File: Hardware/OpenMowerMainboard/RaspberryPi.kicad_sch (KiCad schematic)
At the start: 8 parts, among them J16 Conn_02x03_Odd_Even, J4 RPi_GPIO, M1 Fan, Q3 BSS138, U3 SIP32509DT

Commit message: added footprints to schematic
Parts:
- removed J16: Conn_02x03_Odd_Even, Connector_PinHeader_2.54mm:PinHeader_2x03_P2.54mm_Vertical, symbol Connector_Generic:Conn_02x03_Odd_Even
- removed J4: RPi_GPIO, Connector_PinSocket_2.54mm:PinSocket_2x20_P2.54mm_Vertical_SMD, symbol OpenMowerMainboard-rescue:RPi_GPIO-RPi_Hat
- added J21: Raspberry_Pi_2_3, Connector_PinSocket_2.54mm:PinSocket_2x20_P2.54mm_Vertical_SMD, symbol Connector:Raspberry_Pi_2_3
- added J22: Conn_02x03_Odd_Even, Connector_PinHeader_2.54mm:PinHeader_2x03_P2.54mm_Vertical, symbol Connector_Generic:Conn_02x03_Odd_Even
- D1: footprint (none) -> Diode_SMD:D_SOD-123F
- M1: footprint (none) -> Connector_JST:JST_XH_B2B-XH-A_1x02_P2.50mm_Vertical
- R4, R5: footprint Resistor_SMD:R_0805_2012Metric -> Resistor_SMD:R_0805_2012Metric_Pad1.20x1.40mm_HandSolder
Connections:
- net GND: now also J21.14 (GND), J21.20 (GND), J21.25 (GND), J21.30 (GND), J21.34 (GND), J21.39 (GND), J21.6 (GND), J21.9 (GND)
- net PICO_RESET: now also J22.6 (Pin_6)
- net PICO_SWCLK: now also J22.2 (Pin_2)
- net PICO_SWDIO: now also J22.4 (Pin_4)
- net RASPI_FAN_ON: now also J21.31 (GCLK2/GPIO6)
- net RASPI_POWER: now also J21.2 (5V), J21.4 (5V)
- net UART0_RXD: now also J21.10 (GPIO15/RXD)
- net UART0_TXD: now also J21.8 (GPIO14/TXD)
- net UART1_RXD: now also J21.28 (ID_SC/GPIO1)
- net UART1_TXD: now also J21.27 (ID_SD/GPIO0)
- net UART2_RXD: now also J21.29 (GCLK1/GPIO5)
- net UART2_TXD: now also J21.7 (GCLK0/GPIO4)
- net UART3_RXD: now also J21.21 (MISO0/GPIO9)
- net UART3_TXD: now also J21.24 (~{CE0}/GPIO8)
- net UART4_RXD: now also J21.33 (PWM1/GPIO13)
- net UART4_TXD: now also J21.32 (PWM0/GPIO12)
- new net: J21.22 (GPIO25), J22.1 (Pin_1)
- new net: J21.18 (GPIO24), J22.3 (Pin_3)
- new net: J21.16 (GPIO23), J22.5 (Pin_5)
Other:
- note removed: "Thru-Hole Connector"

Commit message: wip
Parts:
- M1: footprint Connector_JST:JST_XH_B2B-XH-A_1x02_P2.50mm_Vertical -> Connector_PinHeader_2.54mm:PinHeader_1x02_P2.54mm_Vertical
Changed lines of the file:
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@@
       (effects (font (size 1.27 1.27)) (justify left))
     )
-    (property "Footprint" "Connector_JST:JST_XH_B2B-XH-A_1x02_P2.50mm_Vertical" (id 2) (at 116.84 36.576 0)
+    (property "Footprint" "Connector_PinHeader_2.54mm:PinHeader_1x02_P2.54mm_Vertical" (id 2) (at 116.84 36.576 0)
       (effects (font (size 1.27 1.27)) hide)
     )

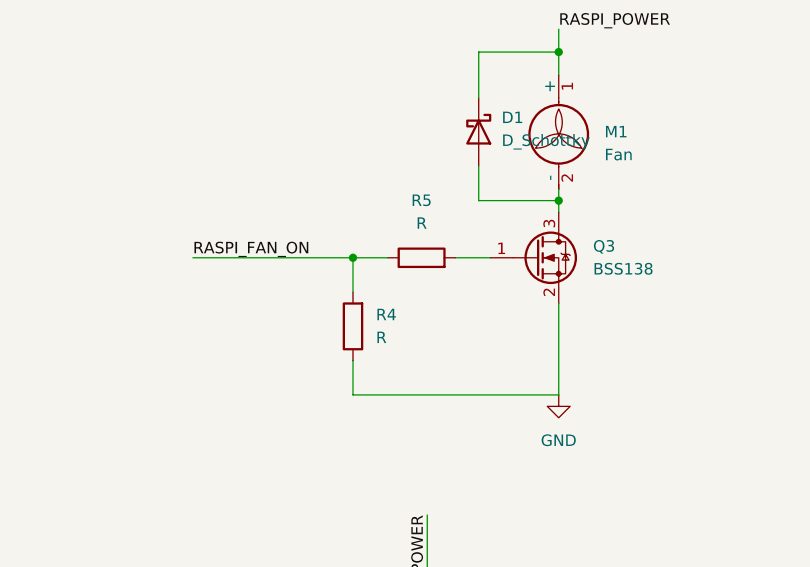
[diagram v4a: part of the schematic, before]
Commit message: update Resistance Values
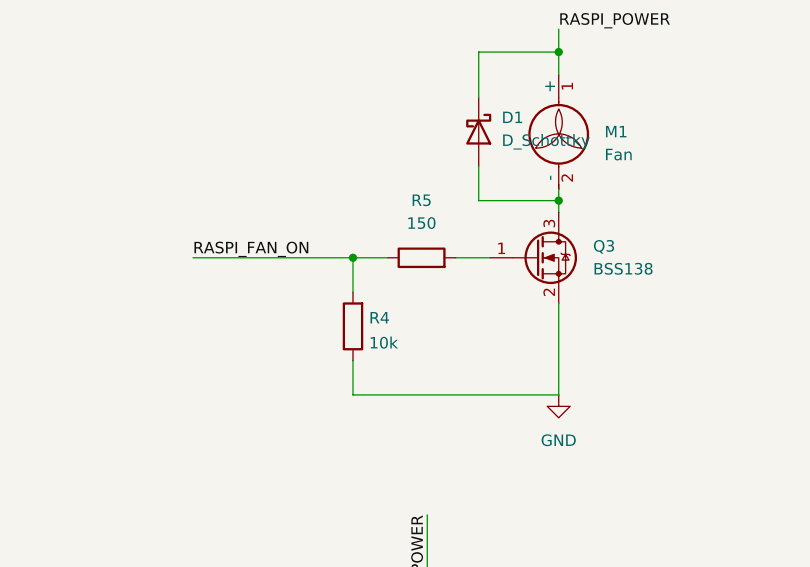
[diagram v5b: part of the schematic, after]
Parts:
- R4: value R -> 10k
- R5: value R -> 150
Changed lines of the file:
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@@
     (in_bom yes) (on_board yes) (fields_autoplaced)
     (property "Reference" "R5" (id 0) (at 101.6 43.18 90))
-    (property "Value" "R" (id 1) (at 101.6 45.72 90))
+    (property "Value" "150" (id 1) (at 101.6 45.72 90))
     (property "Footprint" "Resistor_SMD:R_0805_2012Metric_Pad1.20x1.40mm_HandSolder" (id 2) (at 101.6 51.308 90)
       (effects (font (size 1.27 1.27)) hide)
@@
   (symbol (lib_id "Device:R") (at 93.98 57.15 180) (unit 1)
     (in_bom yes) (on_board yes) (fields_autoplaced)
-    (property "Reference" "R4" (id 0) (at 96.52 55.8799 0)
+    (property "Reference" "R4" (id 0) (at 95.758 56.2415 0)
       (effects (font (size 1.27 1.27)) (justify right))
     )
-    (property "Value" "R" (id 1) (at 96.52 58.4199 0)
+    (property "Value" "10k" (id 1) (at 95.758 59.0166 0)
       (effects (font (size 1.27 1.27)) (justify right))
     )

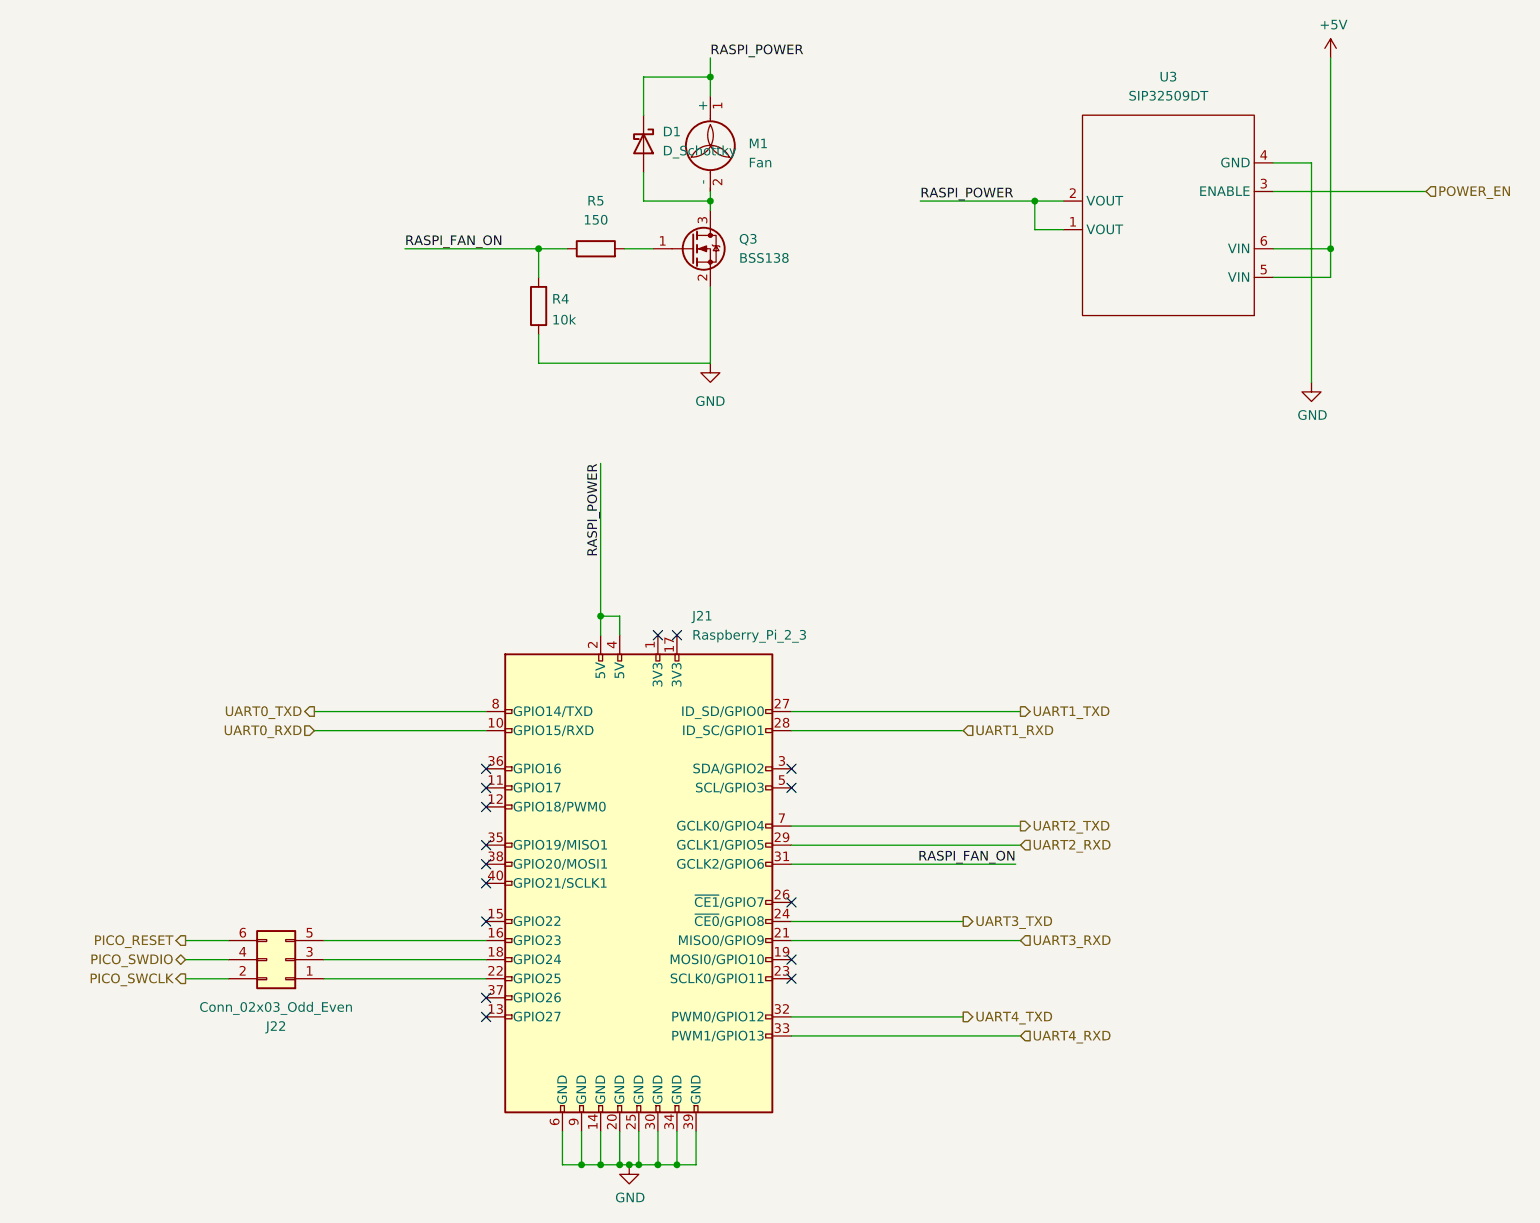
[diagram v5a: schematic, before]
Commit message: Added default pull down, raspberry pi power override and some TODOs
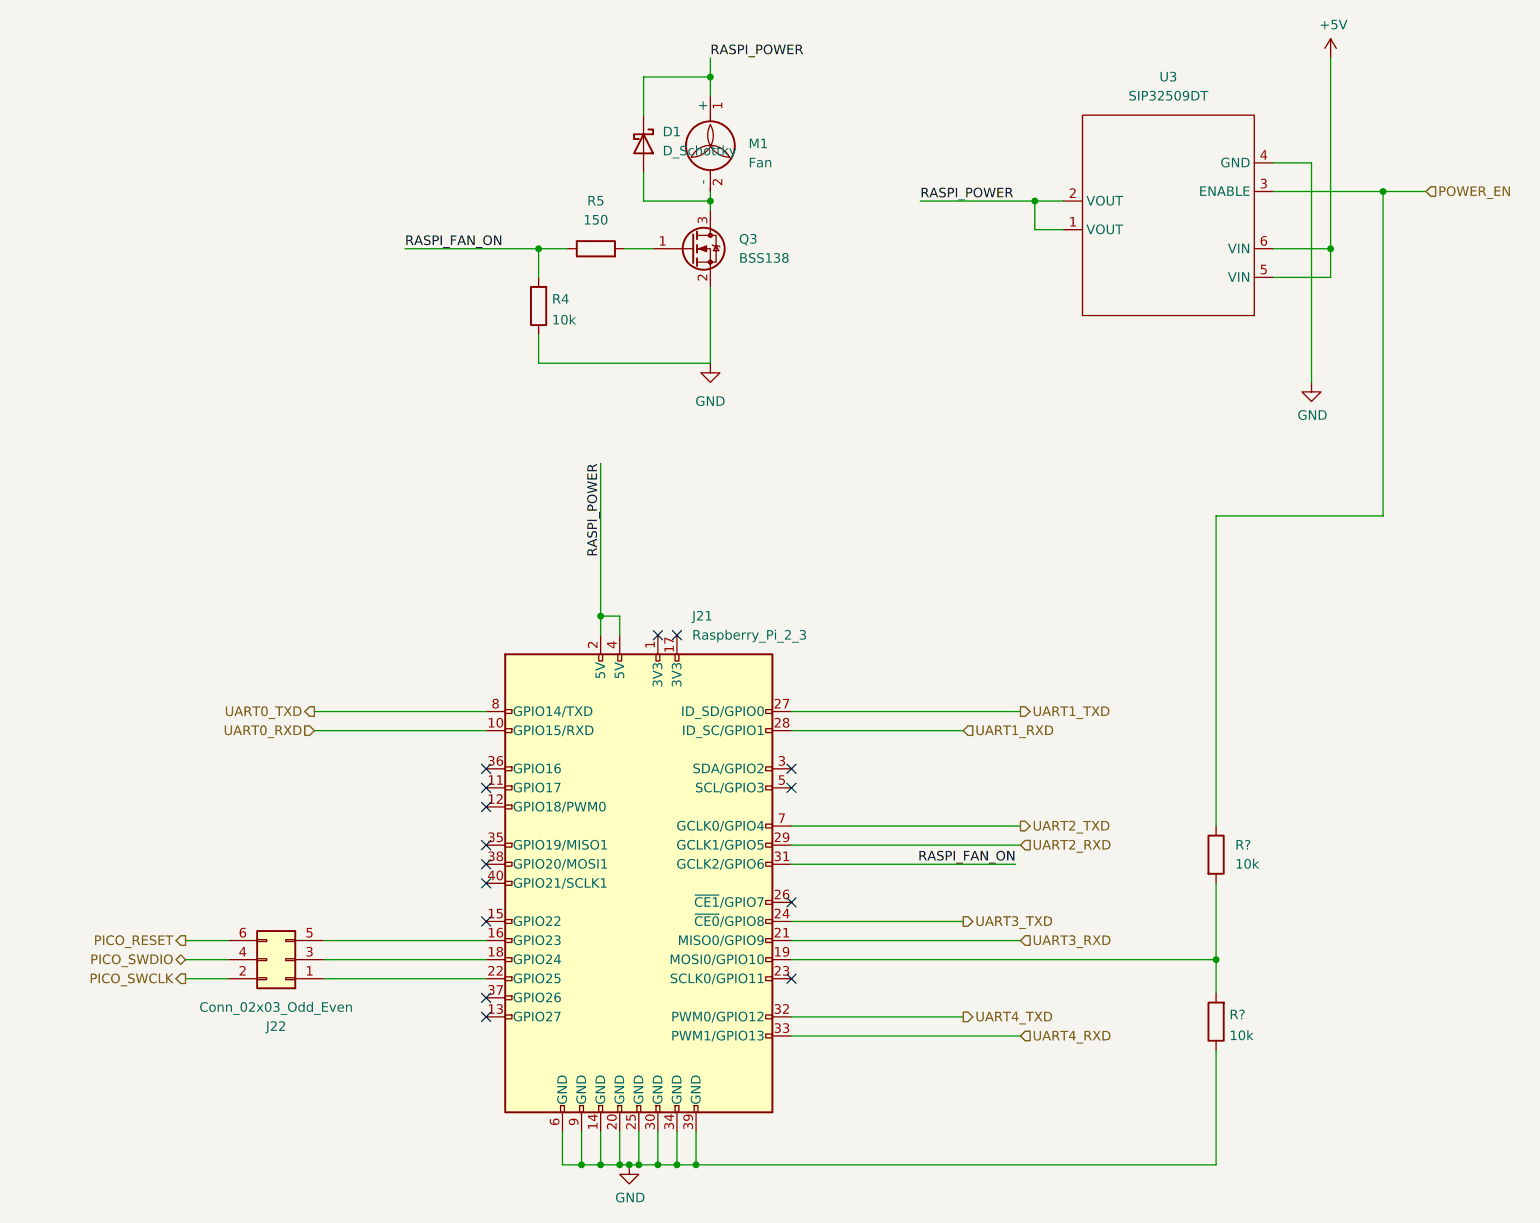
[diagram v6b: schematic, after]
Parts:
- added R? (x2): 10k, Resistor_SMD:R_0805_2012Metric_Pad1.20x1.40mm_HandSolder, symbol Device:R
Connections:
- net GND: now also R?.1
- net POWER_EN: now also R?.1
- net at J21.19 (MOSI0/GPIO10): now also R?.2, R?.2
- no-connect marks 16 -> 15
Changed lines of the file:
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@@
   (junction (at 107.315 171.45) (diameter 0) (color 0 0 0 0)
   )
+  (junction (at 114.935 171.45) (diameter 0) (color 0 0 0 0)
+  )
   (junction (at 109.855 171.45) (diameter 0) (color 0 0 0 0)
   )
@@
   (junction (at 102.235 171.45) (diameter 0) (color 0 0 0 0)
   )
+  (junction (at 184.15 144.145) (diameter 0) (color 0 0 0 0)
+  )
   (junction (at 112.395 171.45) (diameter 0) (color 0 0 0 0)
+  )
+  (junction (at 206.375 41.91) (diameter 0) (color 0 0 0 0)
   )
   (no_connect (at 127.635 121.285))
@@
   (no_connect (at 112.395 100.965))
   (no_connect (at 109.855 100.965))
-  (no_connect (at 127.635 144.145))
   (no_connect (at 86.995 128.905))
   (no_connect (at 86.995 133.985))
@@
     (stroke (width 0) (type default) (color 0 0 0 0))
   )
+  (wire (pts (xy 127.635 144.145) (xy 184.15 144.145))
+    (stroke (width 0) (type default) (color 0 0 0 0))
+  )
   (wire (pts (xy 46.99 141.605) (xy 52.705 141.605))
     (stroke (width 0) (type default) (color 0 0 0 0))
@@
     (stroke (width 0) (type default) (color 0 0 0 0))
   )
-  (wire (pts (xy 191.77 41.91) (xy 212.09 41.91))
+  (wire (pts (xy 184.15 85.09) (xy 184.15 126.365))
+    (stroke (width 0) (type default) (color 0 0 0 0))
+  )
+  (wire (pts (xy 191.77 41.91) (xy 206.375 41.91))
+    (stroke (width 0) (type default) (color 0 0 0 0))
+  )
+  (wire (pts (xy 184.15 85.09) (xy 206.375 85.09))
     (stroke (width 0) (type default) (color 0 0 0 0))
   )
@@
     (stroke (width 0) (type default) (color 0 0 0 0))
   )
+  (wire (pts (xy 184.15 156.21) (xy 184.15 171.45))
+    (stroke (width 0) (type default) (color 0 0 0 0))
+  )
   (wire (pts (xy 104.775 100.965) (xy 104.775 98.425))
     (stroke (width 0) (type default) (color 0 0 0 0))
@@
     (stroke (width 0) (type default) (color 0 0 0 0))
   )
+  (wire (pts (xy 206.375 41.91) (xy 212.09 41.91))
+    (stroke (width 0) (type default) (color 0 0 0 0))
+  )
   (wire (pts (xy 93.98 60.96) (xy 93.98 64.77))
     (stroke (width 0) (type default) (color 0 0 0 0))
@@
     (stroke (width 0) (type default) (color 0 0 0 0))
   )
+  (wire (pts (xy 206.375 85.09) (xy 206.375 41.91))
+    (stroke (width 0) (type default) (color 0 0 0 0))
+  )
+  (wire (pts (xy 184.15 171.45) (xy 114.935 171.45))
+    (stroke (width 0) (type default) (color 0 0 0 0))
+  )
   (wire (pts (xy 158.115 128.905) (xy 127.635 128.905))
     (stroke (width 0) (type default) (color 0 0 0 0))
   )
+  (wire (pts (xy 184.15 144.145) (xy 184.15 148.59))
+    (stroke (width 0) (type default) (color 0 0 0 0))
+  )
   (wire (pts (xy 97.155 171.45) (xy 99.695 171.45))
+    (stroke (width 0) (type default) (color 0 0 0 0))
+  )
+  (wire (pts (xy 184.15 133.985) (xy 184.15 144.145))
     (stroke (width 0) (type default) (color 0 0 0 0))
   )
@@
     )
     (property "Datasheet" "~" (id 3) (at 107.95 35.56 0)
+      (effects (font (size 1.27 1.27)) hide)
+    )
+    (pin "1")
+    (pin "2")
+  )
+  (symbol (lib_id "Device:R") (at 184.15 152.4 180) (unit 1)
+    (in_bom yes) (on_board yes) (fields_autoplaced)
+    (property "Reference" "R?" (id 0) (at 185.928 151.4915 0)
+      (effects (font (size 1.27 1.27)) (justify right))
+    )
+    (property "Value" "10k" (id 1) (at 185.928 154.2666 0)
+      (effects (font (size 1.27 1.27)) (justify right))
+    )
+    (property "Footprint" "Resistor_SMD:R_0805_2012Metric_Pad1.20x1.40mm_HandSolder" (id 2) (at 185.928 152.4 90)
+      (effects (font (size 1.27 1.27)) hide)
+    )
+    (property "Datasheet" "~" (id 3) (at 184.15 152.4 0)
       (effects (font (size 1.27 1.27)) hide)
     )
@@
     (pin "9")
   )
+  (symbol (lib_id "Device:R") (at 184.15 130.175 0) (unit 1)
+    (in_bom yes) (on_board yes) (fields_autoplaced)
+    (property "Reference" "R?" (id 0) (at 186.69 128.9049 0)
+      (effects (font (size 1.27 1.27)) (justify left))
+    )
+    (property "Value" "10k" (id 1) (at 186.69 131.4449 0)
+      (effects (font (size 1.27 1.27)) (justify left))
+    )
+    (property "Footprint" "Resistor_SMD:R_0805_2012Metric_Pad1.20x1.40mm_HandSolder" (id 2) (at 182.372 130.175 90)
+      (effects (font (size 1.27 1.27)) hide)
+    )
+    (property "Datasheet" "~" (id 3) (at 184.15 130.175 0)
+      (effects (font (size 1.27 1.27)) hide)
+    )
+    (pin "1")
+    (pin "2")
+  )
   (symbol (lib_id "power:GND") (at 116.84 64.77 0) (unit 1)

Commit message: WIP hardware revision
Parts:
- gave numbers to parts that had none: 2
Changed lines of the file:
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@@
   (symbol (lib_id "Device:R") (at 184.15 152.4 180) (unit 1)
     (in_bom yes) (on_board yes) (fields_autoplaced)
-    (property "Reference" "R?" (id 0) (at 185.928 151.4915 0)
+    (property "Reference" "R2" (id 0) (at 185.928 151.4915 0)
       (effects (font (size 1.27 1.27)) (justify right))
     )
@@
   (symbol (lib_id "Device:R") (at 184.15 130.175 0) (unit 1)
     (in_bom yes) (on_board yes) (fields_autoplaced)
-    (property "Reference" "R?" (id 0) (at 186.69 128.9049 0)
+    (property "Reference" "R1" (id 0) (at 186.69 128.9049 0)
       (effects (font (size 1.27 1.27)) (justify left))
     )
